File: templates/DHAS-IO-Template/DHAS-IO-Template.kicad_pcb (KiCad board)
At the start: 4 copper layers, 42.2 x 42.2 mm, 7 parts, among them J1 Conn_01x09_Male, J2_bot1 Conn_02x20_Odd_Even, J2_top1 Conn_02x20_Odd_Even

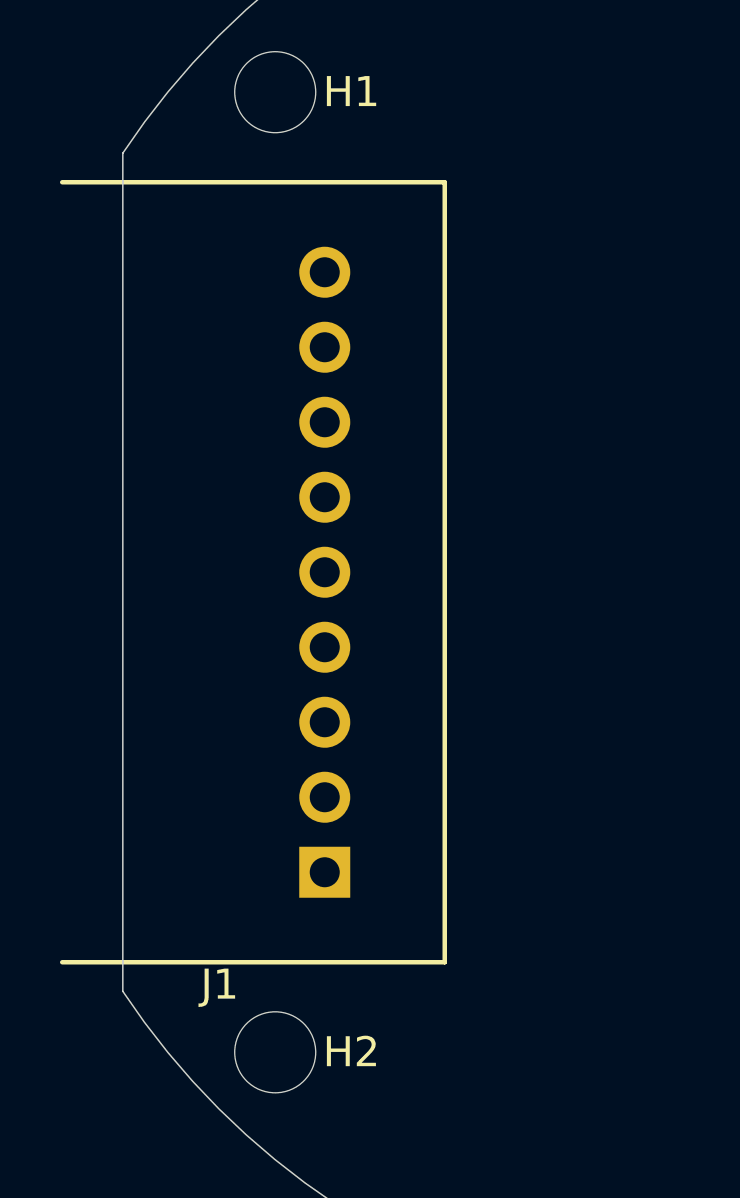
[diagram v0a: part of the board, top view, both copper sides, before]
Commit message: update template with fixed connector footprint
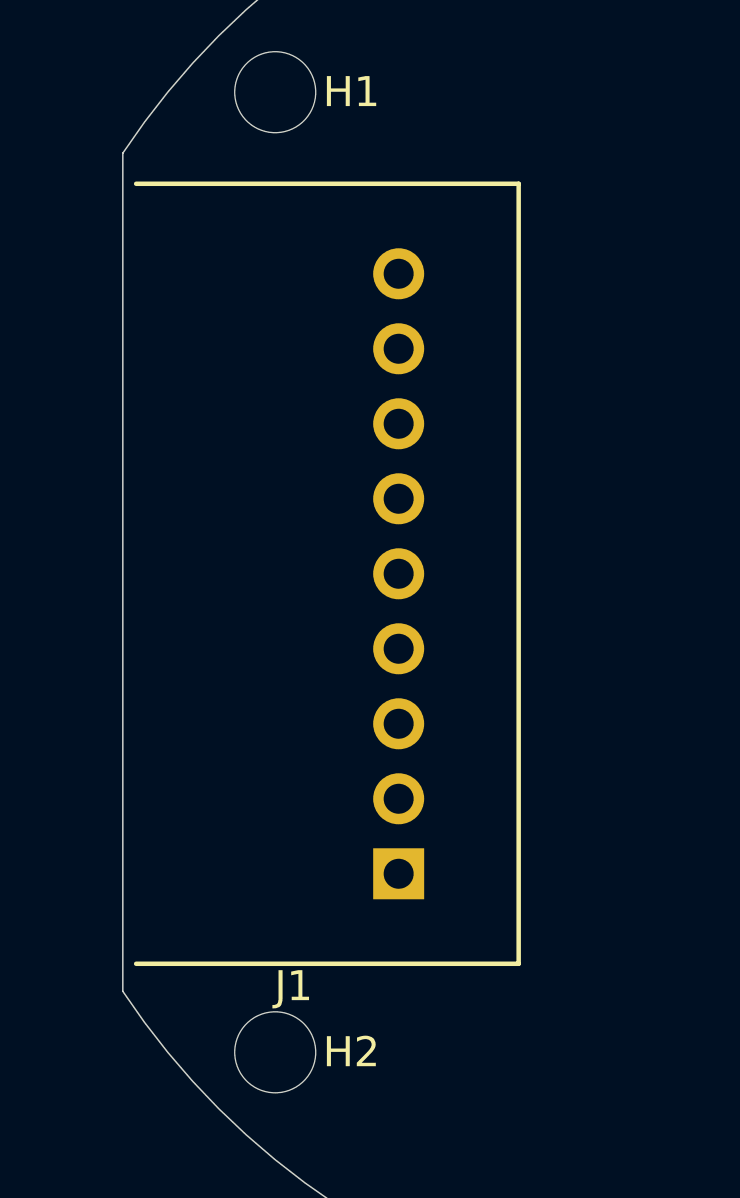
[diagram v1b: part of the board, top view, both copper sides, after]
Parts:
- J1: footprint DHAS:TE_EP2.5_9p_Horizontal -> Connector_TE-Connectivity.DHAS:TE_EP2.5_9p_Horizontal
- moved J1 2.46 mm to (79.6, 66.1)
